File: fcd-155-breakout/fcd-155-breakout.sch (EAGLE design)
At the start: 2 parts, among them X1 RJ45-8X-E5908

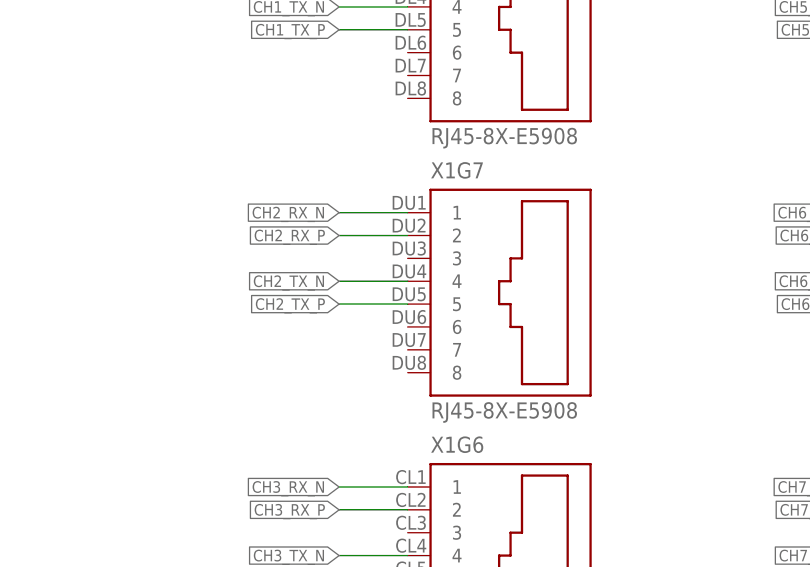
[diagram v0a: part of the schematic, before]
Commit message: fcd-155-breakout: Fix pin-out for even numbered ports
Related: OS#6678
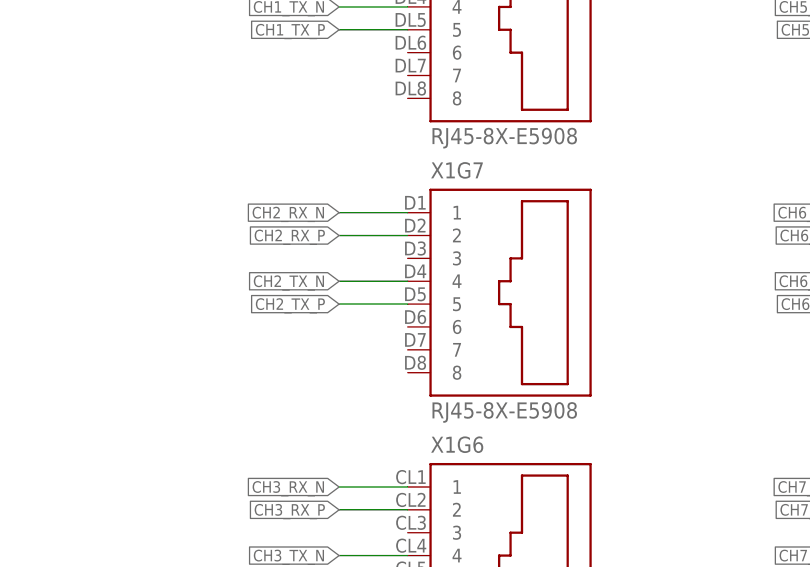
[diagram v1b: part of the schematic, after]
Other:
- moved on the sheet: X1G7
